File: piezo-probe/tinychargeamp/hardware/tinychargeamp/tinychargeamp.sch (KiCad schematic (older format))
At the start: 9 parts, among them J1 Conn_01x02, J2 Conn_01x03, J3 Conn_01x02, U1 ATtiny13A-SSU

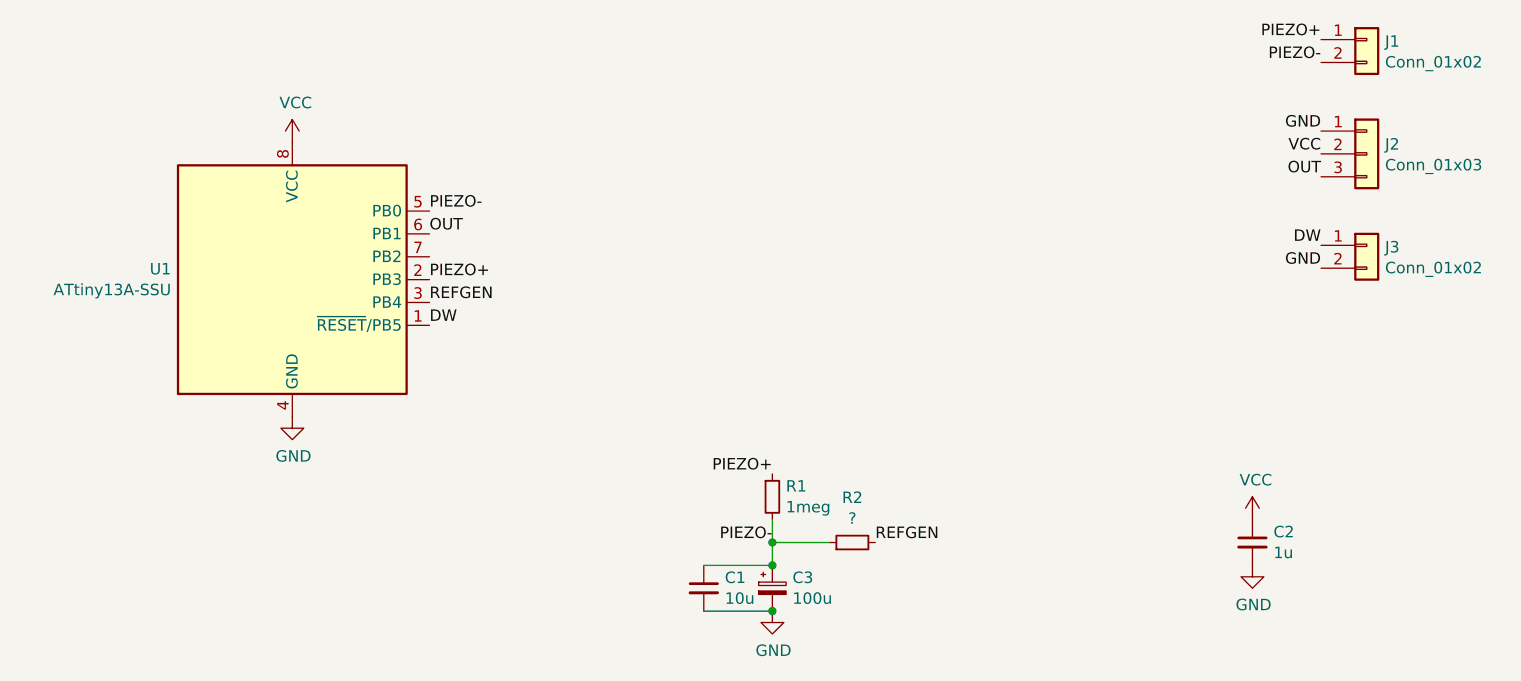
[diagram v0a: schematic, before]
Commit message: Update board and firmware
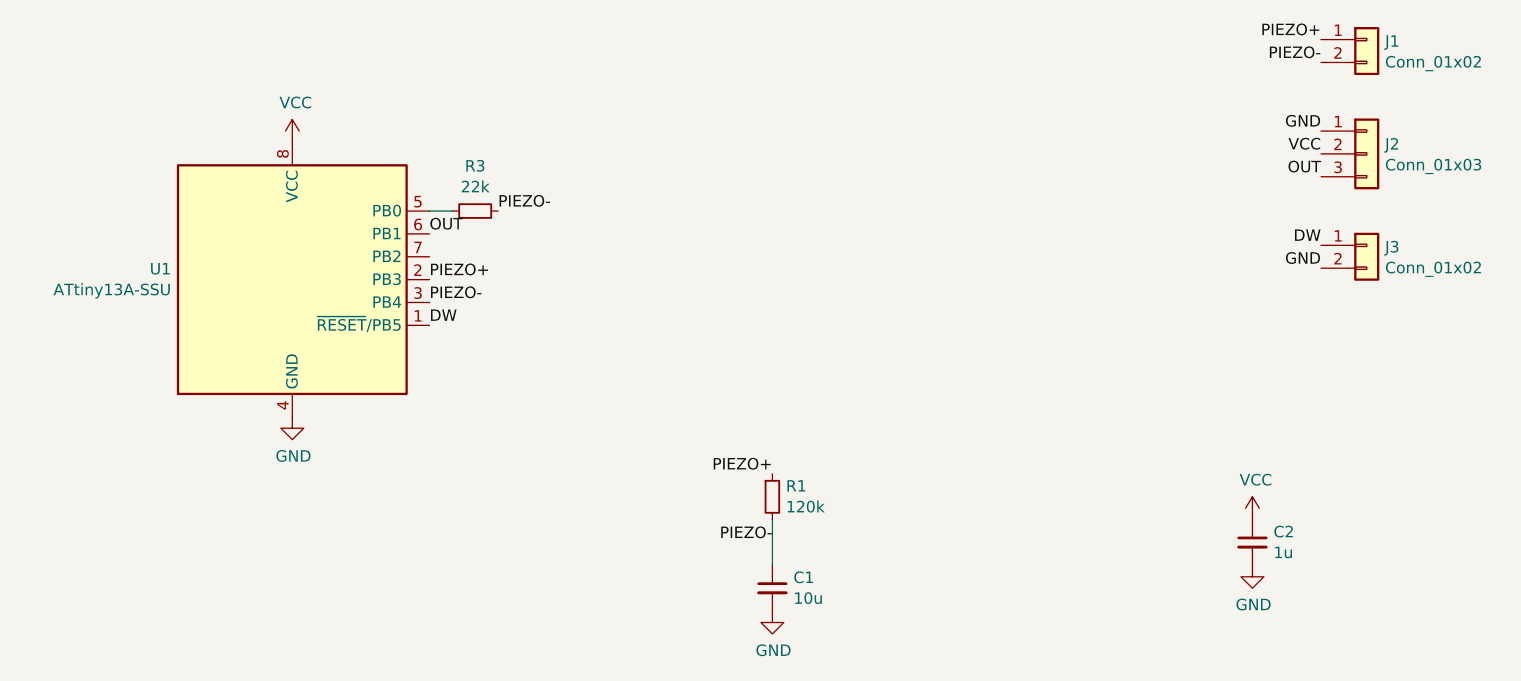
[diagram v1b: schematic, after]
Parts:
- removed C3: 100u, Capacitor_Tantalum_SMD:CP_EIA-3528-15_AVX-H, symbol Device:CP_Small
- removed R2: ?, Resistor_SMD:R_1206_3216Metric_Pad1.42x1.75mm_HandSolder, symbol Device:R_Small
- added R3: 22k, Resistor_SMD:R_1206_3216Metric_Pad1.42x1.75mm_HandSolder, symbol Device:R_Small
- R1: value 1meg -> 120k
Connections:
- net REFGEN is gone; now on net PIEZO-: U1.3 (PB4)
- net PIEZO-: now also R3.2; no longer U1.5 (PB0)
- new net: R3.1, U1.5 (PB0)
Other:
- moved on the sheet: C1
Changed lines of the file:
@@
 P 7000 3450
 F 0 "R1" H 7059 3496 50  0000 L CNN
-F 1 "1meg" H 7059 3405 50  0000 L CNN
+F 1 "120k" H 7059 3405 50  0000 L CNN
 F 2 "Resistor_SMD:R_1206_3216Metric_Pad1.42x1.75mm_HandSolder" H 7000 3450 50  0001 C CNN
 F 3 "~" H 7000 3450 50  0001 C CNN
@@
 	1    9600 1950
 	1    0    0    -1
-$EndComp
-$Comp
-L Device:R_Small R2
-U 1 1 5EF36A3A
-P 7350 3650
-F 0 "R2" V 7546 3650 50  0000 C CNN
-F 1 "?" V 7455 3650 50  0000 C CNN
-F 2 "Resistor_SMD:R_1206_3216Metric_Pad1.42x1.75mm_HandSolder" H 7350 3650 50  0001 C CNN
-F 3 "~" H 7350 3650 50  0001 C CNN
-	1    7350 3650
-	0    -1   -1   0
 $EndComp
 $Comp
@@
 	1    0    0    -1
 $EndComp
-Wire Wire Line
-	7250 3650 7000 3650
-Wire Wire Line
-	7000 3650 7000 3550
-Wire Wire Line
-	7000 3650 7000 3750
-Connection ~ 7000 3650
 $Comp
 L power:GND #PWR0105
@@
 Text Label 7000 3650 2    50   ~ 0
 PIEZO-
-Text Label 7450 3650 0    50   ~ 0
-REFGEN
-Text Label 5500 2600 0    50   ~ 0
-REFGEN
 Text Label 5500 2500 0    50   ~ 0
 PIEZO+
-Text Label 5500 2200 0    50   ~ 0
+Text Label 5800 2200 0    50   ~ 0
 PIEZO-
 Text Label 5500 2300 0    50   ~ 0
@@
 DW
 $Comp
-L Device:CP_Small C3
-U 1 1 5EF49C6A
+L Device:C_Small C1
+U 1 1 5EF4B09A
 P 7000 3850
-F 0 "C3" H 7088 3896 50  0000 L CNN
-F 1 "100u" H 7088 3805 50  0000 L CNN
-F 2 "Capacitor_Tantalum_SMD:CP_EIA-3528-15_AVX-H" H 7000 3850 50  0001 C CNN
+F 0 "C1" H 7092 3896 50  0000 L CNN
+F 1 "10u" H 7092 3805 50  0000 L CNN
+F 2 "Capacitor_SMD:C_0805_2012Metric_Pad1.15x1.40mm_HandSolder" H 7000 3850 50  0001 C CNN
 F 3 "~" H 7000 3850 50  0001 C CNN
 	1    7000 3850
@@
 $EndComp
 $Comp
-L Device:C_Small C1
-U 1 1 5EF4B09A
-P 6700 3850
-F 0 "C1" H 6792 3896 50  0000 L CNN
-F 1 "10u" H 6792 3805 50  0000 L CNN
-F 2 "Capacitor_SMD:C_0805_2012Metric_Pad1.15x1.40mm_HandSolder" H 6700 3850 50  0001 C CNN
-F 3 "~" H 6700 3850 50  0001 C CNN
-	1    6700 3850
-	1    0    0    -1
+L Device:R_Small R3
+U 1 1 5EFB8AF6
+P 5700 2200
+F 0 "R3" V 5896 2200 50  0000 C CNN
+F 1 "22k" V 5805 2200 50  0000 C CNN
+F 2 "Resistor_SMD:R_1206_3216Metric_Pad1.42x1.75mm_HandSolder" H 5700 2200 50  0001 C CNN
+F 3 "~" H 5700 2200 50  0001 C CNN
+	1    5700 2200
+	0    -1   -1   0
 $EndComp
 Wire Wire Line
-	6700 3750 7000 3750
-Connection ~ 7000 3750
+	5500 2200 5600 2200
+Text Label 5500 2600 0    50   ~ 0
+PIEZO-
 Wire Wire Line
-	6700 3950 7000 3950
-Connection ~ 7000 3950
+	7000 3550 7000 3750
 $EndSCHEMATC
